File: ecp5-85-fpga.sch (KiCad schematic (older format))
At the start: 1 part

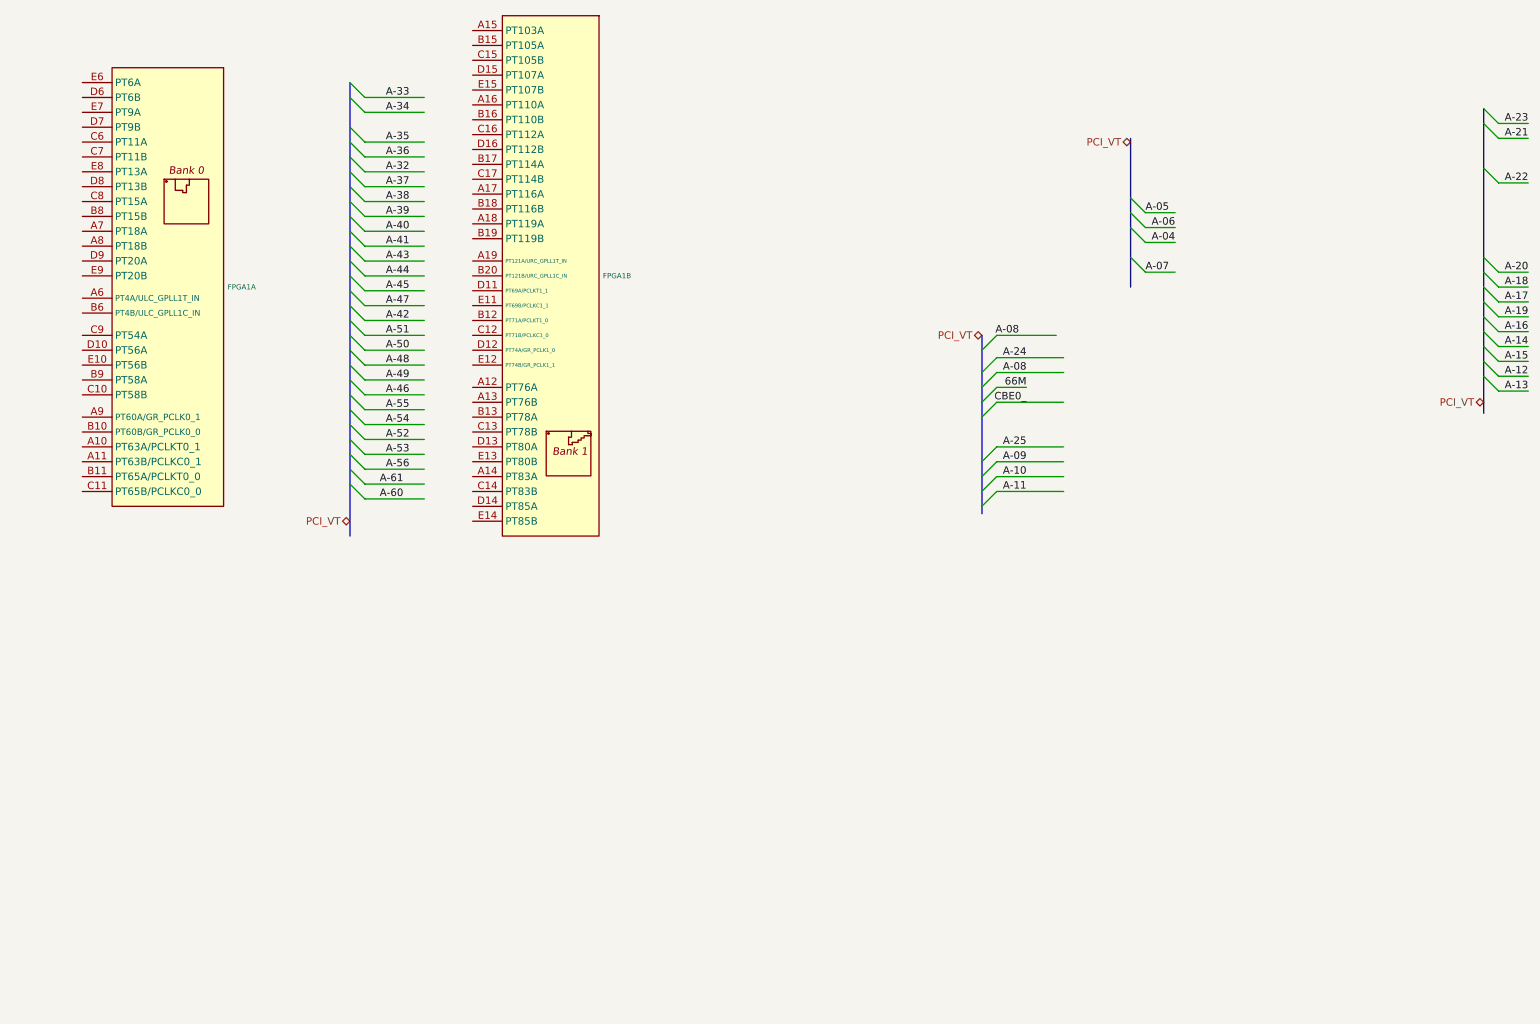
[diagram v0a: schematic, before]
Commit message: Add files via upload
Added Pull-up and pull-down resistors for JTAG and sysConfig connections.
Added pinheaders for FPGA-Configuration. (replacing edge-connector)
Combined the DVI+VGA and USB-C hierarchical sheets into one.
Assigned a dedicated sheet for the DAC.
Added 75 Ohm terminal-resistors to output of DAC.
Placed filtering-capacitors for DAC VAA.
Connected VGA ID-bits and DVI DDC together.
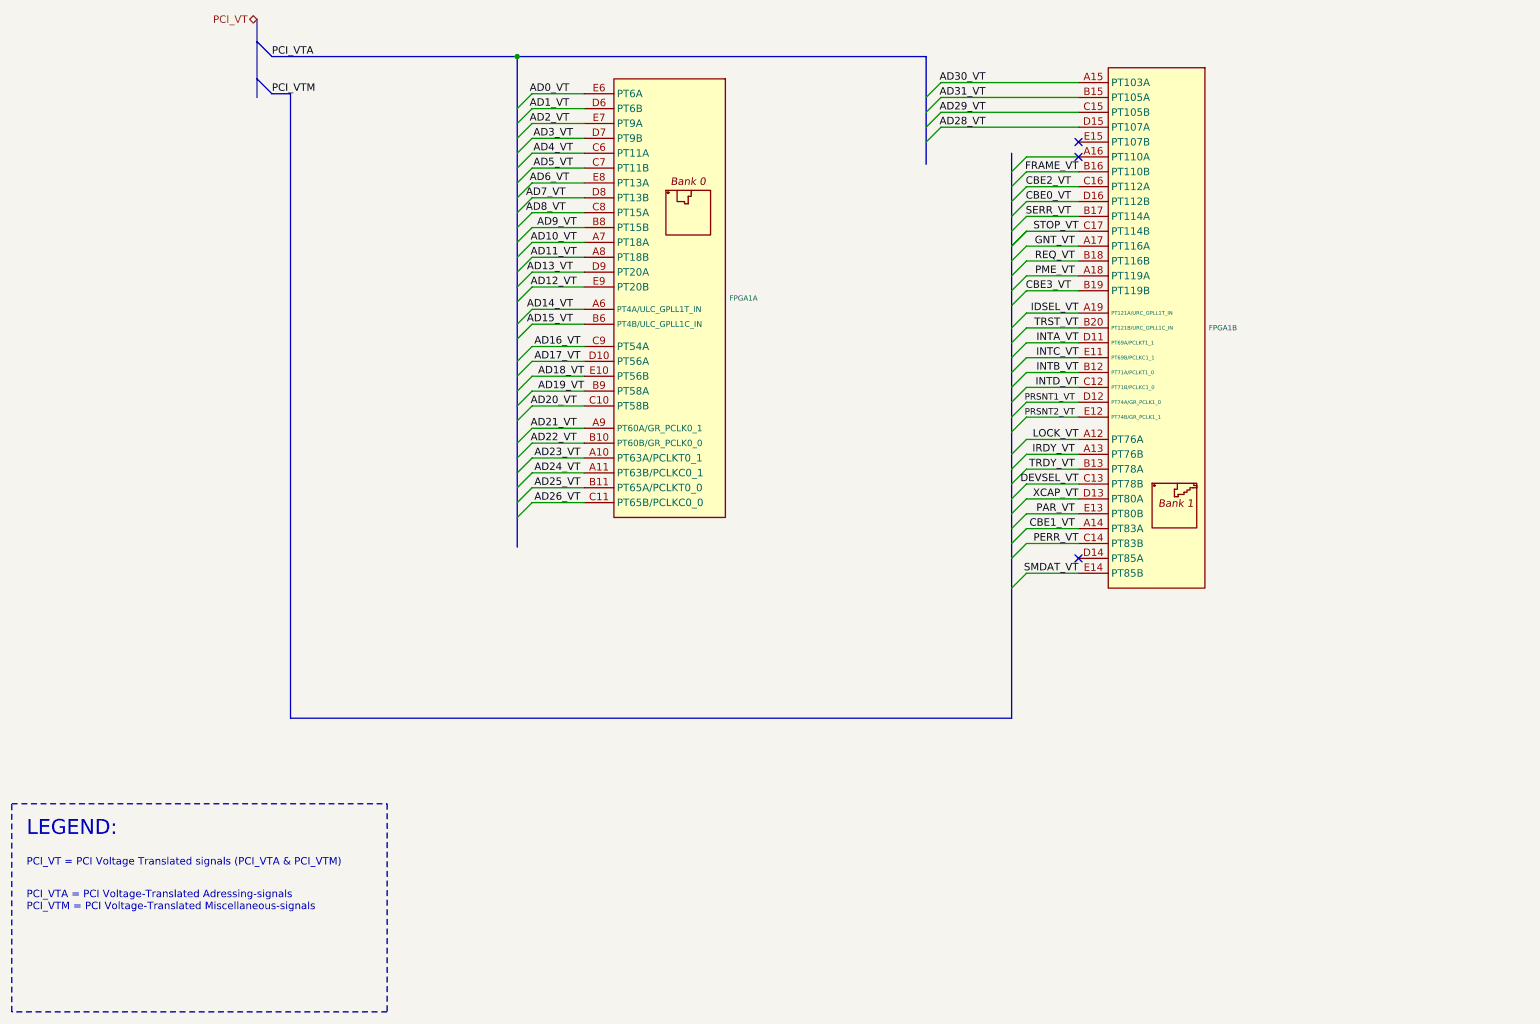
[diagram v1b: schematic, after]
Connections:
- net labels added: AD0_VT, AD10_VT, AD11_VT, AD12_VT, AD13_VT, AD14_VT, AD15_VT, AD16_VT, AD17_VT, AD18_VT, AD19_VT, AD1_VT, AD20_VT, AD21_VT, AD22_VT, AD23_VT, AD24_VT, AD25_VT, AD26_VT, AD28_VT, AD29_VT, AD2_VT, AD30_VT, AD31_VT, AD3_VT, AD4_VT, AD5_VT, AD6_VT, AD7_VT, AD8_VT, AD9_VT, CBE0_VT, CBE1_VT, CBE2_VT, CBE3_VT, DEVSEL_VT, FRAME_VT, GNT_VT, IDSEL_VT, INTA_VT, INTB_VT, INTC_VT, INTD_VT, IRDY_VT, LOCK_VT, PAR_VT, PCI_VTA, PCI_VTM, PERR_VT, PME_VT, PRSNT1_VT, PRSNT2_VT, REQ_VT, SERR_VT, SMDAT_VT, STOP_VT, TRDY_VT, TRST_VT, XCAP_VT
- net labels removed: 66M, A-04, A-05, A-06, A-07, A-08, A-09, A-10, A-11, A-12, A-13, A-14, A-15, A-16, A-17, A-18, A-19, A-20, A-21, A-22, A-23, A-24, A-25, A-32, A-33, A-34, A-35, A-36, A-37, A-38, A-39, A-40, A-41, A-42, A-43, A-44, A-45, A-46, A-47, A-48, A-49, A-50, A-51, A-52, A-53, A-54, A-55, A-56, A-60, A-61, CBE0_
- wire segments 52 -> 58
- no-connect marks 0 -> 3
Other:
- note added: "LEGEND:"
- note added: "PCI_VT = PCI Voltage Translated signals (PCI_VTA & PCI_VTM)"
- note added: "PCI_VTA = PCI Voltage-Translated Adressing-signals\nPCI_VTM = PCI Voltage-Translated Miscellaneous-signals"
- moved on the sheet: FPGA1A, FPGA1B

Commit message: Add files via upload
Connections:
- net M66EN_VT: now reaches FPGA1.E15 (PT107B)
- no-connect marks 3 -> 1
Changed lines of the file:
@@
 Wire Wire Line
 	4625 2450 4275 2450
-Entry Wire Line
-	7600 1775 7500 1875
 Wire Wire Line
 	4275 1350 4625 1350
@@
 Wire Wire Line
 	7950 2175 7600 2175
-Wire Wire Line
-	7950 1775 7600 1775
 $Comp
 L LRJ-parts:LFE5U-85F-BG381-LRJ FPGA?
@@
 	6925 1100 4175 1100
 Connection ~ 4175 1100
-NoConn ~ 7950 1675
 NoConn ~ 7950 4475
 Entry Wire Line
@@
 Wire Wire Line
 	7950 2275 7600 2275
-NoConn ~ 7950 1775
 Wire Notes Line
 	3300 6125 3300 7525
@@
 Text Notes 875  6350 0    100  ~ 0
 LEGEND:
+Entry Wire Line
+	7600 1675 7500 1775
+Entry Wire Line
+	7600 1675 7500 1775
+Text Label 7950 1675 2    50   ~ 0
+M66EN_VT
+Wire Wire Line
+	7950 1675 7600 1675
 Wire Bus Line
 	2425 850  2425 1375
